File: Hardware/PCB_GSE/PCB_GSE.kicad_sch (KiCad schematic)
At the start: 38 parts, among them J1 Conn_01x06_Pin, U1 STM32F103CBT6

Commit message: wip : routing local circuits and power planes
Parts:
- removed R6: 22R, Resistor_SMD:R_0603_1608Metric, symbol Device:R_Small
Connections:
- no-connect marks 0 -> 1
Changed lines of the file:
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@@
 		(color 0 0 0 0)
 	)
+	(no_connect
+		(at 130.81 68.58)
+	)
 	(wire
 		(pts
@@
 	(wire
 		(pts
-			(xy 123.19 68.58) (xy 124.46 68.58)
-		)
-		(stroke
-			(width 0)
-			(type default)
-		)
-	)
-	(wire
-		(pts
 			(xy 151.13 43.18) (xy 148.59 43.18)
 		)
@@
 	(wire
 		(pts
-			(xy 129.54 68.58) (xy 130.81 68.58)
-		)
-		(stroke
-			(width 0)
-			(type default)
-		)
-	)
-	(wire
-		(pts
 			(xy 148.59 43.18) (xy 146.05 43.18)
 		)
@@
 		)
 	)
-	(global_label "ISO_CAN_OUT"
-		(shape input)
-		(at 123.19 68.58 180)
-		(fields_autoplaced yes)
-		(effects
-			(font
-				(size 1.27 1.27)
-			)
-			(justify right)
-		)
-		(property "Intersheetrefs" "${INTERSHEET_REFS}"
-			(at 107.8071 68.58 0)
-			(effects
-				(font
-					(size 1.27 1.27)
-				)
-				(justify right)
-				(hide yes)
-			)
-		)
-	)
 	(global_label "Pressure_Sleep"
 		(shape input)
@@
 					(unit 1)
 				)
-			)
-		)
-	)
-	(symbol
-		(lib_id "Device:R_Small")
-		(at 127 68.58 90)
-		(unit 1)
-		(exclude_from_sim no)
-		(in_bom yes)
-		(on_board yes)
-		(dnp no)
-		(property "Reference" "R6"
-			(at 105.918 68.58 90)
-			(effects
-				(font
-					(size 1.016 1.016)
-				)
-				(justify left)
-			)
-		)
-		(property "Value" "22R"
-			(at 102.616 68.58 90)
-			(effects
-				(font
-					(size 1.27 1.27)
-				)
-				(justify left)
-			)
-		)
-		(property "Footprint" "Resistor_SMD:R_0603_1608Metric"
-			(at 127 68.58 0)
-			(effects
-				(font
-					(size 1.27 1.27)
-				)
-				(hide yes)
-			)
-		)
-		(property "Datasheet" "https://www.digikey.ca/en/products/detail/rohm-semiconductor/ESR03EZPJ220/1983463"
-			(at 127 68.58 0)
-			(effects
-				(font
-					(size 1.27 1.27)
-				)
-				(hide yes)
-			)
-		)
-		(property "Description" "Resistor, small symbol"
-			(at 127 68.58 0)
-			(effects
-				(font
-					(size 1.27 1.27)
-				)
-				(hide yes)
-			)
-		)
-		(property "DigiKey_Part_Number" "RHM22DCT-ND"
-			(at 127 68.58 90)
-			(effects
-				(font
-					(size 1.27 1.27)
-				)
-				(hide yes)
-			)
-		)
-		(property "Manufacturer_Part_Number" "ESR03EZPJ220"
-			(at 127 68.58 90)
-			(effects
-				(font
-					(size 1.27 1.27)
-				)
-				(hide yes)
-			)
-		)
-		(pin "1"
-		)
-		(pin "2"
-		)
-		(instances
-			(project "PCB_GSE"
-				(path "/a63f9ed4-21e4-42d0-8bfc-f96143f84d4d"
-					(reference "R6")
-					(unit 1)
-				)

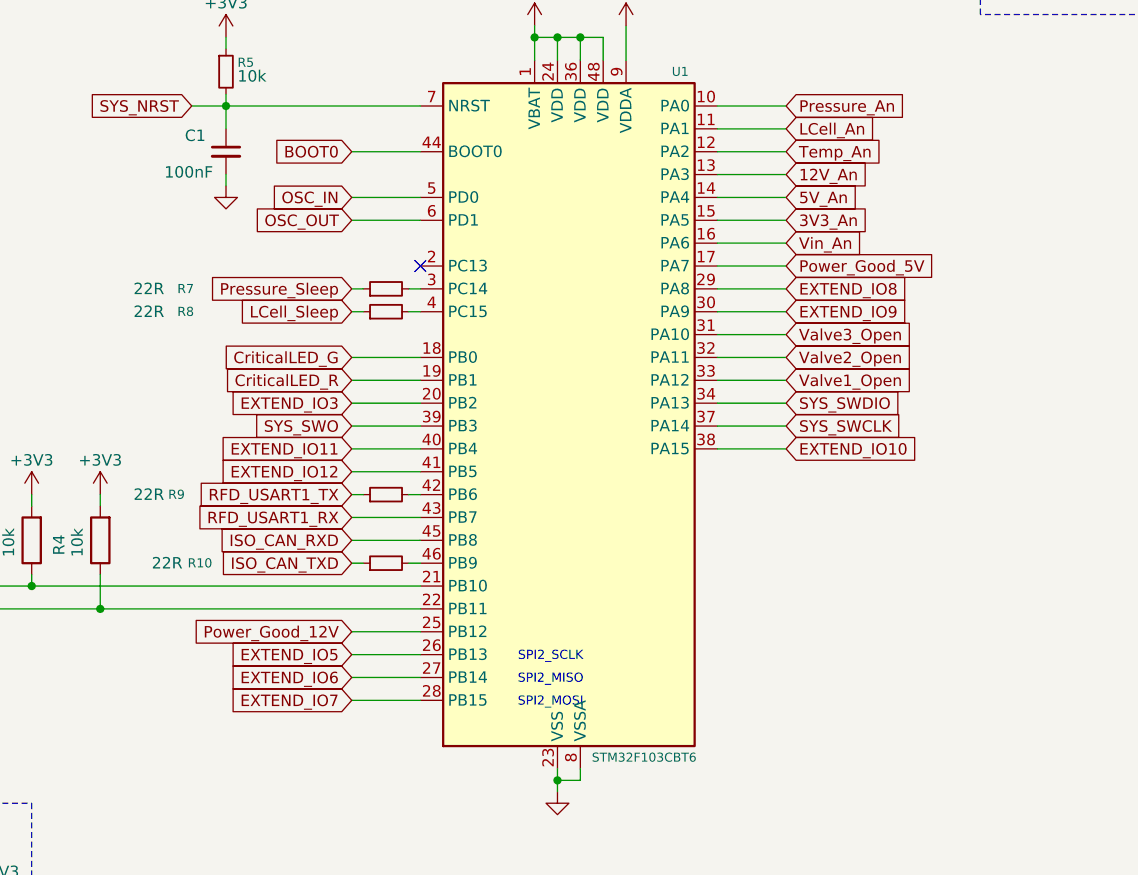
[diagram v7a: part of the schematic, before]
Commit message: fix(gse & moteur): mapping + routing, remove CAN_ISO_IN/OUT
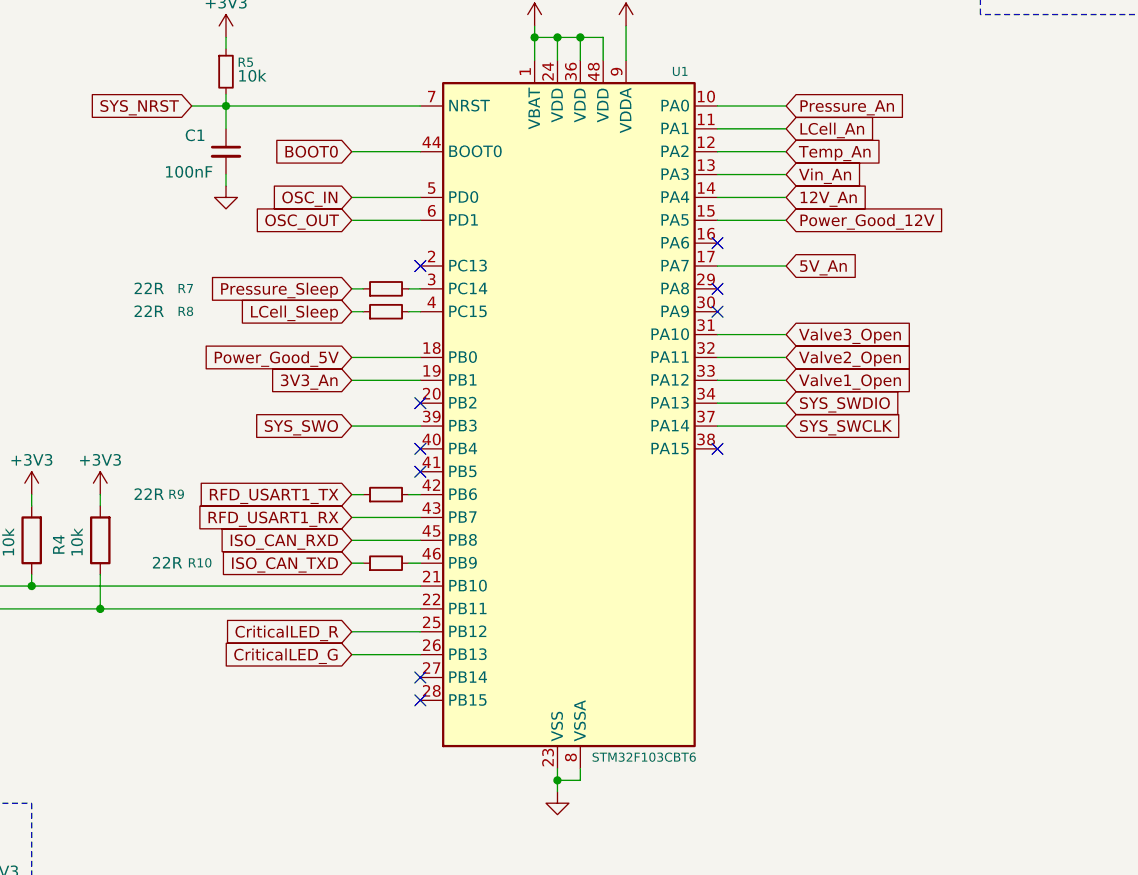
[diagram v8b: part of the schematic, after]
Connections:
- net EXTEND_IO5 is gone; now on net CriticalLED_G: U1.26 (PB13)
- net 12V_An: now also U1.14 (PA4); no longer U1.13 (PA3)
- net 3V3_An: now also U1.19 (PB1); no longer U1.15 (PA5)
- net 5V_An: now also U1.17 (PA7); no longer U1.14 (PA4)
- net CriticalLED_G: no longer U1.18 (PB0)
- net CriticalLED_R: now also U1.25 (PB12); no longer U1.19 (PB1)
- net Power_Good_12V: now also U1.15 (PA5); no longer U1.25 (PB12)
- net Power_Good_5V: now also U1.18 (PB0); no longer U1.17 (PA7)
- net Vin_An: now also U1.13 (PA3); no longer U1.16 (PA6)
- net EXTEND_IO10: no longer names the net of U1.38 (PA15)
- net EXTEND_IO11: no longer names the net of U1.40 (PB4)
- net EXTEND_IO12: no longer names the net of U1.41 (PB5)
- net EXTEND_IO3: no longer names the net of U1.20 (PB2)
- net EXTEND_IO6: no longer names the net of U1.27 (PB14)
- net EXTEND_IO7: no longer names the net of U1.28 (PB15)
- net EXTEND_IO8: no longer names the net of U1.29 (PA8)
- net EXTEND_IO9: no longer names the net of U1.30 (PA9)
- no-connect marks 1 -> 10
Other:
- note removed: "SPI2_MISO"
- note removed: "SPI2_MOSI"
- note removed: "SPI2_SCLK"
